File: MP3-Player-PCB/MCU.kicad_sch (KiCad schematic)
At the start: 8 parts, among them J201 Conn_ARM_SWD_TagConnect_TC2030, U201 STM32F411CEUx

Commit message: Up to date
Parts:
- added C207: 100n, symbol Device:C
- added C208: 4.7u, symbol Device:C
- added R201: 10k, symbol Device:R
- C201: value 10u -> 4.7u
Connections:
- net GND: now also U201.23 (VSS), U201.35 (VSS), U201.47 (VSS), U201.49 (VSS), U201.8 (VSSA), C207.2, C208.2, R201.1
- net at U201.22 (VCAP1): now also C208.1
- net BOOT: now reaches U201.44 (BOOT0)
- net BOOT: now also R201.2
- net NRST: now reaches U201.7 (NRST)
- net NRST: now also C207.1

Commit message: Started power schematic
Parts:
- renumbered C201 to C101, C202 to C102, C203 to C103, C204 to C104, C205 to C105, C206 to C106, C207 to C107, C208 to C108, J201 to J101, R201 to R101, U201 to U101
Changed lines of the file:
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@@
 		(dnp no)
 		(fields_autoplaced yes)
-		(property "Reference" "C203"
+		(property "Reference" "C103"
 			(at 63.5 44.4499 0)
 			(effects
@@
 			(project ""
 				(path "/3f51ea9b-d2e1-4711-a47c-269e1b97e0f4/94b81035-f90d-4565-a117-ac4535135684"
-					(reference "C203")
+					(reference "C103")
 					(unit 1)
 				)
@@
 		(dnp no)
 		(fields_autoplaced yes)
-		(property "Reference" "#PWR0206"
+		(property "Reference" "#PWR0105"
 			(at 81.28 147.32 0)
 			(effects
@@
 			(project "MP3-Player"
 				(path "/3f51ea9b-d2e1-4711-a47c-269e1b97e0f4/94b81035-f90d-4565-a117-ac4535135684"
-					(reference "#PWR0206")
+					(reference "#PWR0105")
 					(unit 1)
 				)
@@
 		(on_board yes)
 		(dnp no)
-		(property "Reference" "R201"
+		(property "Reference" "R101"
 			(at 83.82 65.278 90)
 			(effects
@@
 			(project ""
 				(path "/3f51ea9b-d2e1-4711-a47c-269e1b97e0f4/94b81035-f90d-4565-a117-ac4535135684"
-					(reference "R201")
+					(reference "R101")
 					(unit 1)
 				)
@@
 		(dnp no)
 		(fields_autoplaced yes)
-		(property "Reference" "U201"
+		(property "Reference" "U101"
 			(at 115.1733 138.43 0)
 			(effects
@@
 				)
 				(path "/3f51ea9b-d2e1-4711-a47c-269e1b97e0f4/94b81035-f90d-4565-a117-ac4535135684"
-					(reference "U201")
+					(reference "U101")
 					(unit 1)
 				)
@@
 		(dnp no)
 		(fields_autoplaced yes)
-		(property "Reference" "C206"
+		(property "Reference" "C106"
 			(at 97.79 44.4499 0)
 			(effects
@@
 			(project ""
 				(path "/3f51ea9b-d2e1-4711-a47c-269e1b97e0f4/94b81035-f90d-4565-a117-ac4535135684"
-					(reference "C206")
+					(reference "C106")
 					(unit 1)
 				)
@@
 		(dnp no)
 		(fields_autoplaced yes)
-		(property "Reference" "J201"
+		(property "Reference" "J101"
 			(at 207.01 66.0399 0)
 			(effects
@@
 			(project ""
 				(path "/3f51ea9b-d2e1-4711-a47c-269e1b97e0f4/94b81035-f90d-4565-a117-ac4535135684"
-					(reference "J201")
+					(reference "J101")
 					(unit 1)
 				)
@@
 		(dnp no)
 		(fields_autoplaced yes)
-		(property "Reference" "#PWR0204"
+		(property "Reference" "#PWR0103"
 			(at 72.39 80.01 0)
 			(effects
@@
 			(project "MP3-Player"
 				(path "/3f51ea9b-d2e1-4711-a47c-269e1b97e0f4/94b81035-f90d-4565-a117-ac4535135684"
-					(reference "#PWR0204")
+					(reference "#PWR0103")
 					(unit 1)
 				)
@@
 		(dnp no)
 		(fields_autoplaced yes)
-		(property "Reference" "#PWR0201"
+		(property "Reference" "#PWR0102"
 			(at 36.83 59.69 0)
 			(effects
@@
 			(project ""
 				(path "/3f51ea9b-d2e1-4711-a47c-269e1b97e0f4/94b81035-f90d-4565-a117-ac4535135684"
-					(reference "#PWR0201")
+					(reference "#PWR0102")
 					(unit 1)
 				)
@@
 		(dnp no)
 		(fields_autoplaced yes)
-		(property "Reference" "#PWR0203"
+		(property "Reference" "#PWR0106"
 			(at 110.49 147.32 0)
 			(effects
@@
 			(project ""
 				(path "/3f51ea9b-d2e1-4711-a47c-269e1b97e0f4/94b81035-f90d-4565-a117-ac4535135684"
-					(reference "#PWR0203")
+					(reference "#PWR0106")
 					(unit 1)
 				)
@@
 		(dnp no)
 		(fields_autoplaced yes)
-		(property "Reference" "C205"
+		(property "Reference" "C105"
 			(at 86.36 44.4499 0)
 			(effects
@@
 			(project ""
 				(path "/3f51ea9b-d2e1-4711-a47c-269e1b97e0f4/94b81035-f90d-4565-a117-ac4535135684"
-					(reference "C205")
+					(reference "C105")
 					(unit 1)
 				)
@@
 		(dnp no)
 		(fields_autoplaced yes)
-		(property "Reference" "C202"
+		(property "Reference" "C102"
 			(at 52.07 44.4499 0)
 			(effects
@@
 			(project ""
 				(path "/3f51ea9b-d2e1-4711-a47c-269e1b97e0f4/94b81035-f90d-4565-a117-ac4535135684"
-					(reference "C202")
+					(reference "C102")
 					(unit 1)
 				)
@@
 		(dnp no)
 		(fields_autoplaced yes)
-		(property "Reference" "C208"
+		(property "Reference" "C108"
 			(at 85.09 134.6199 0)
 			(effects
@@
 			(project "MP3-Player"
 				(path "/3f51ea9b-d2e1-4711-a47c-269e1b97e0f4/94b81035-f90d-4565-a117-ac4535135684"
-					(reference "C208")
+					(reference "C108")
 					(unit 1)
 				)
@@
 		(dnp no)
 		(fields_autoplaced yes)
-		(property "Reference" "C204"
+		(property "Reference" "C104"
 			(at 74.93 44.4499 0)
 			(effects
@@
 			(project ""
 				(path "/3f51ea9b-d2e1-4711-a47c-269e1b97e0f4/94b81035-f90d-4565-a117-ac4535135684"
-					(reference "C204")
+					(reference "C104")
 					(unit 1)
 				)
@@
 		(dnp no)
 		(fields_autoplaced yes)
-		(property "Reference" "#PWR0202"
+		(property "Reference" "#PWR0101"
 			(at 36.83 40.64 0)
 			(effects
@@
 			(project ""
 				(path "/3f51ea9b-d2e1-4711-a47c-269e1b97e0f4/94b81035-f90d-4565-a117-ac4535135684"
-					(reference "#PWR0202")
+					(reference "#PWR0101")
 					(unit 1)
 				)
@@
 		(dnp no)
 		(fields_autoplaced yes)
-		(property "Reference" "C201"
+		(property "Reference" "C101"
 			(at 40.64 44.4499 0)
 			(effects
@@
 			(project ""
 				(path "/3f51ea9b-d2e1-4711-a47c-269e1b97e0f4/94b81035-f90d-4565-a117-ac4535135684"
-					(reference "C201")
+					(reference "C101")
 					(unit 1)
 				)
@@
 		(on_board yes)
 		(dnp no)
-		(property "Reference" "C207"
+		(property "Reference" "C107"
 			(at 63.754 67.31 0)
 			(effects
@@
 			(project "MP3-Player"
 				(path "/3f51ea9b-d2e1-4711-a47c-269e1b97e0f4/94b81035-f90d-4565-a117-ac4535135684"
-					(reference "C207")
+					(reference "C107")
 					(unit 1)
 				)
@@
 		(dnp no)
 		(fields_autoplaced yes)
-		(property "Reference" "#PWR0205"
+		(property "Reference" "#PWR0104"
 			(at 78.74 80.01 0)
 			(effects
@@
 			(project "MP3-Player"
 				(path "/3f51ea9b-d2e1-4711-a47c-269e1b97e0f4/94b81035-f90d-4565-a117-ac4535135684"
-					(reference "#PWR0205")
-					(unit 1)
-				)
+					(reference "#PWR0104")
+					(unit 1)
+				)

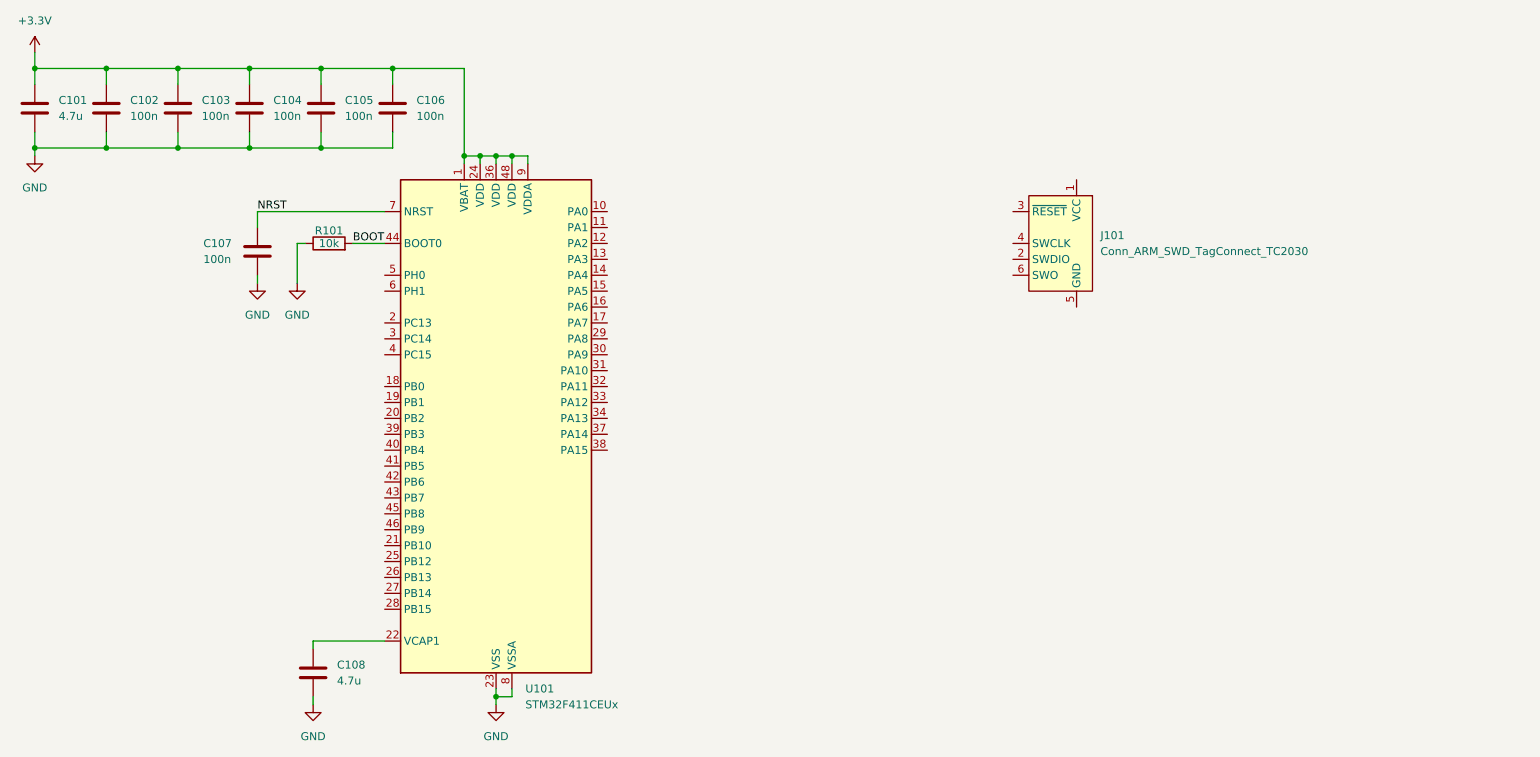
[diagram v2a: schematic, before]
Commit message: Added charger IC schematic circuitry
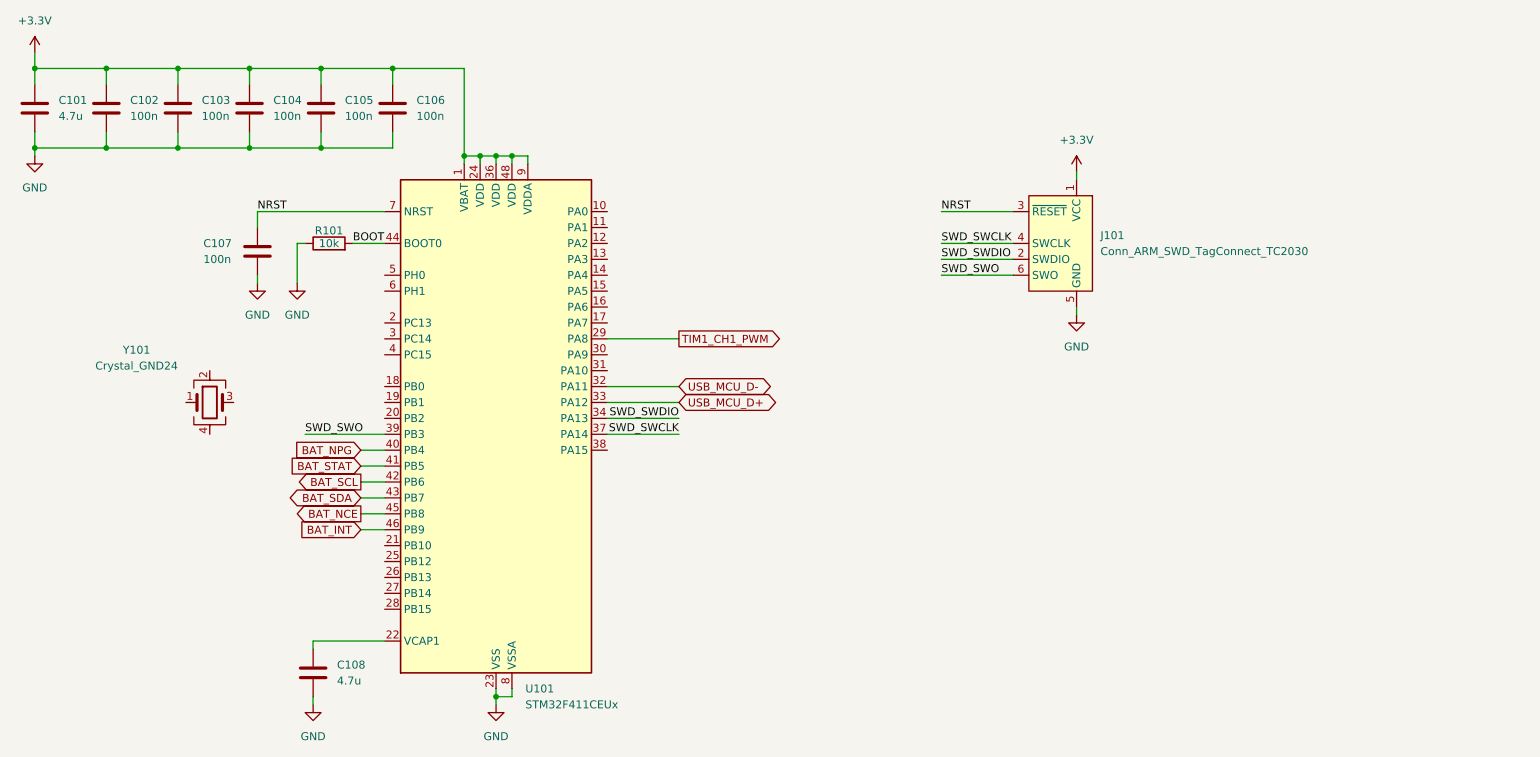
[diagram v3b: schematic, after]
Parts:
- added Y101: Crystal_GND24, symbol Device:Crystal_GND24
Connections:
- net +3.3V: now also J101.1 (VCC)
- net GND: now also J101.5 (GND)
- net NRST: now also J101.3 (~{RESET})
- net TIM1_CH1_PWM: now reaches U101.29 (PA8)
- net USB_MCU_D-: now reaches U101.32 (PA11)
- net USB_MCU_D+: now reaches U101.33 (PA12)
- net SWD_SWDIO: now reaches U101.34 (PA13)
- net SWD_SWDIO: now also J101.2 (SWDIO)
- net SWD_SWCLK: now reaches U101.37 (PA14)
- net SWD_SWCLK: now also J101.4 (SWCLK)
- net SWD_SWO: now reaches U101.39 (PB3)
- net SWD_SWO: now also J101.6 (SWO)
- net BAT_NPG: now reaches U101.40 (PB4)
- net BAT_STAT: now reaches U101.41 (PB5)
- net BAT_SCL: now reaches U101.42 (PB6)
- net BAT_SDA: now reaches U101.43 (PB7)
- net BAT_NCE: now reaches U101.45 (PB8)
- net BAT_INT: now reaches U101.46 (PB9)

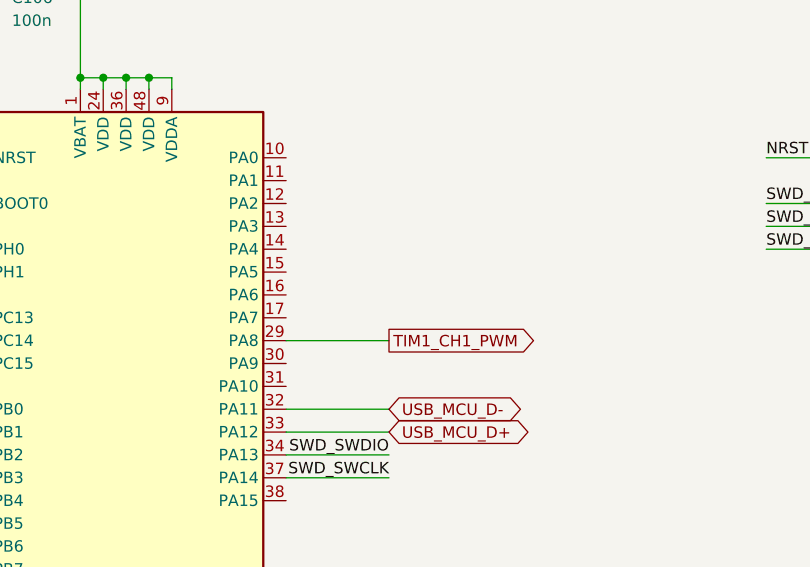
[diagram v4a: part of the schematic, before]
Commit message: Finished SD card connections with MCU
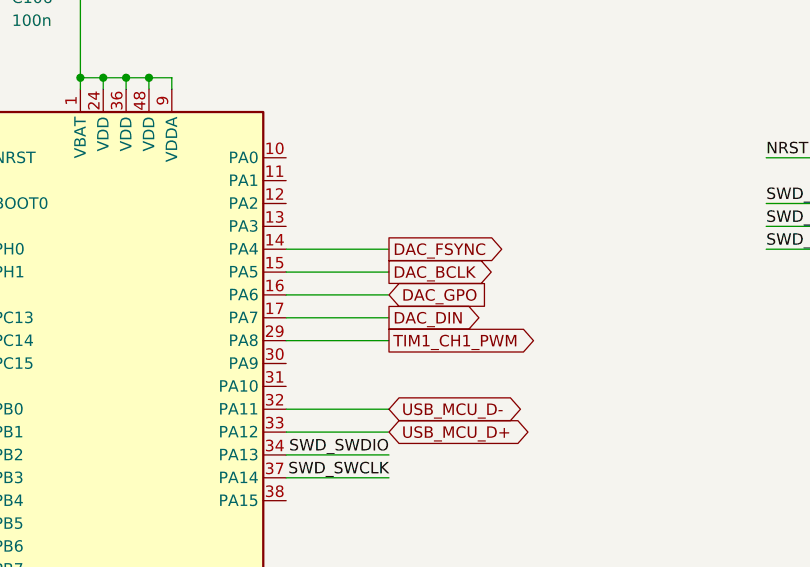
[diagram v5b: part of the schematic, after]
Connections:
- net DAC_FSYNC: now reaches U101.14 (PA4)
- net DAC_BCLK: now reaches U101.15 (PA5)
- net DAC_GPO: now reaches U101.16 (PA6)
- net DAC_DIN: now reaches U101.17 (PA7)
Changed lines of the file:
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@@
+	(wire
+		(pts
+			(xy 128.27 74.93) (xy 139.7 74.93)
+		)
+		(stroke
+			(width 0)
+			(type default)
+		)
+	)
 	(wire
 		(pts
@@
 	(wire
 		(pts
+			(xy 128.27 72.39) (xy 139.7 72.39)
+		)
+		(stroke
+			(width 0)
+			(type default)
+		)
+	)
+	(wire
+		(pts
 			(xy 88.9 102.87) (xy 92.71 102.87)
 		)
@@
 		(pts
 			(xy 81.28 139.7) (xy 81.28 140.97)
+		)
+		(stroke
+			(width 0)
+			(type default)
+		)
+	)
+	(wire
+		(pts
+			(xy 128.27 80.01) (xy 139.7 80.01)
+		)
+		(stroke
+			(width 0)
+			(type default)
+		)
+	)
+	(wire
+		(pts
+			(xy 128.27 77.47) (xy 139.7 77.47)
 		)
 		(stroke
@@
 		)
 	)
+	(global_label "DAC_FSYNC"
+		(shape output)
+		(at 139.7 72.39 0)
+		(fields_autoplaced yes)
+		(effects
+			(font
+				(size 1.27 1.27)
+			)
+			(justify left)
+		)
+		(property "Intersheetrefs" "${INTERSHEET_REFS}"
+			(at 153.2686 72.39 0)
+			(effects
+				(font
+					(size 1.27 1.27)
+				)
+				(justify left)
+				(hide yes)
+			)
+		)
+	)
 	(global_label "BAT_SDA"
 		(shape bidirectional)
@@
 		)
 	)
+	(global_label "DAC_GPO"
+		(shape input)
+		(at 139.7 77.47 0)
+		(fields_autoplaced yes)
+		(effects
+			(font
+				(size 1.27 1.27)
+			)
+			(justify left)
+		)
+		(property "Intersheetrefs" "${INTERSHEET_REFS}"
+			(at 151.1519 77.47 0)
+			(effects
+				(font
+					(size 1.27 1.27)
+				)
+				(justify left)
+				(hide yes)
+			)
+		)
+	)
 	(global_label "TIM1_CH1_PWM"
 		(shape output)
@@
 		)
 	)
+	(global_label "DAC_DIN"
+		(shape output)
+		(at 139.7 80.01 0)
+		(fields_autoplaced yes)
+		(effects
+			(font
+				(size 1.27 1.27)
+			)
+			(justify left)
+		)
+		(property "Intersheetrefs" "${INTERSHEET_REFS}"
+			(at 150.4867 80.01 0)
+			(effects
+				(font
+					(size 1.27 1.27)
+				)
+				(justify left)
+				(hide yes)
+			)
+		)
+	)
 	(global_label "BAT_INT"
 		(shape input)
@@
 				(hide yes)
 			)
+		)
+	)
+	(global_label "DAC_BCLK"
+		(shape output)
+		(at 139.7 74.93 0)
+		(fields_autoplaced yes)
+		(effects
+			(font
+				(size 1.27 1.27)
+			)
+			(justify left)
+		)
+		(property "Intersheetrefs" "${INTERSHEET_REFS}"
+			(at 152.1195 74.93 0)
+			(effects
+				(font
+					(size 1.27 1.27)
+				)
+				(justify left)
+				(hide yes)
+			)

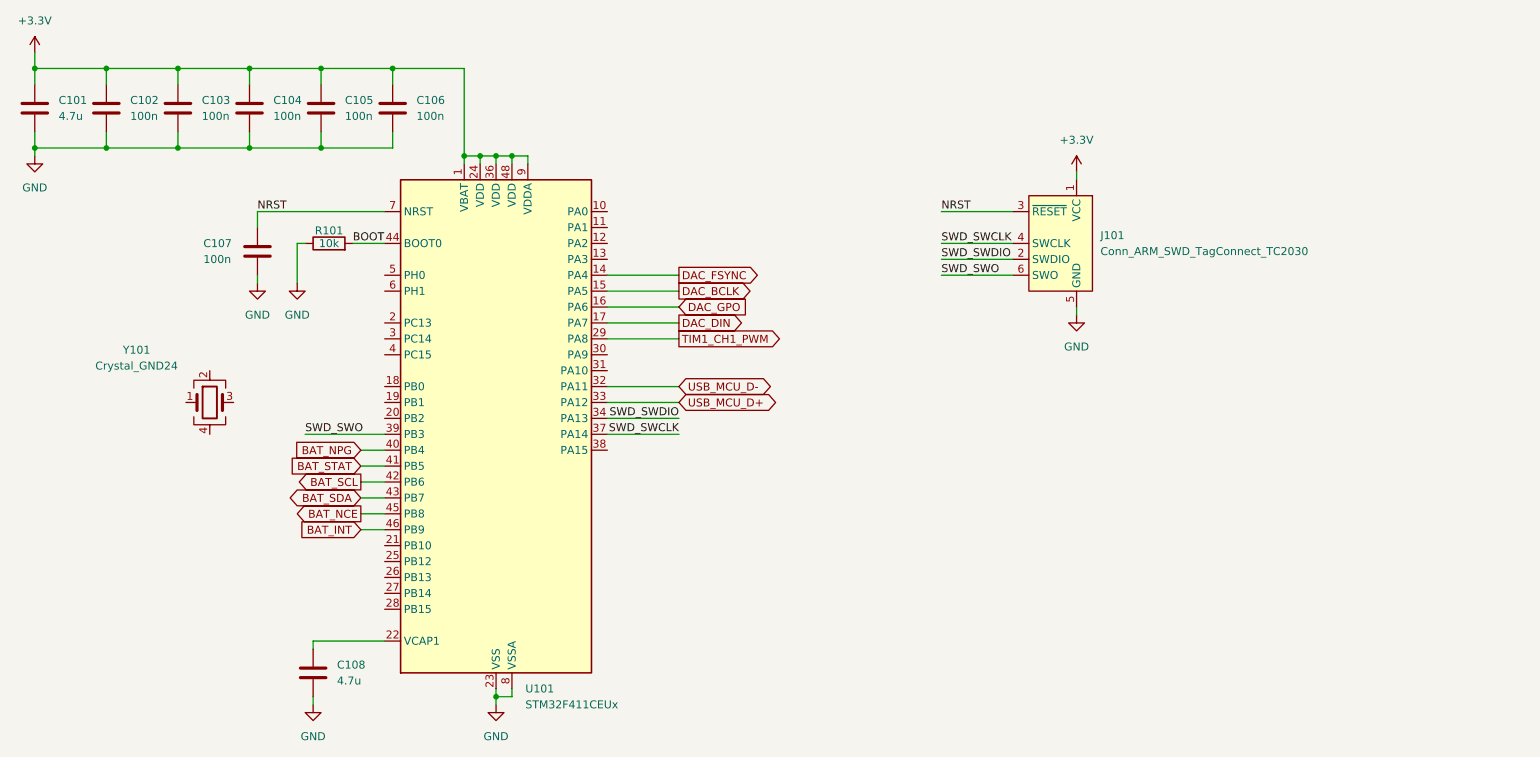
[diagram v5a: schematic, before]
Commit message: Added addressable LED circuitry
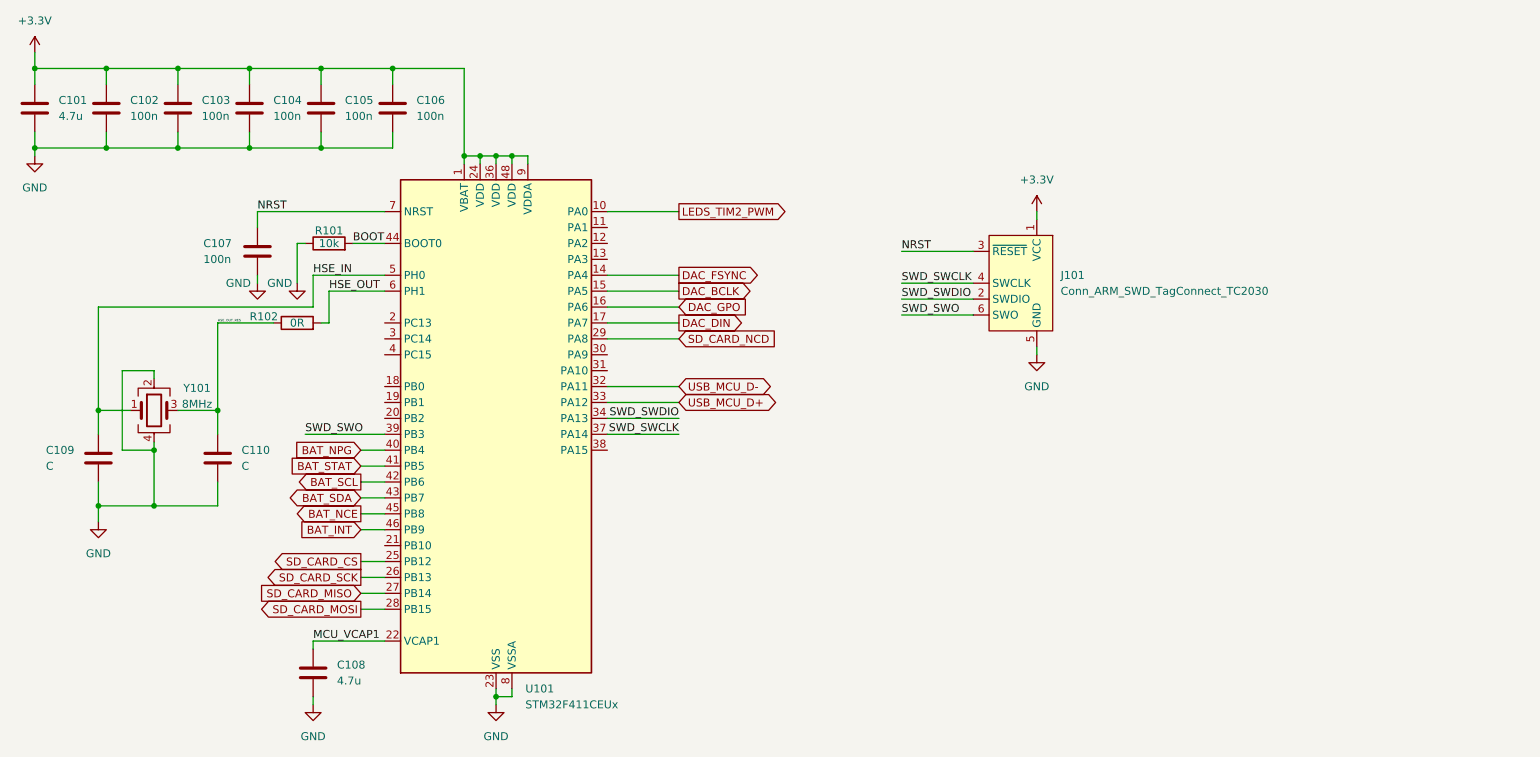
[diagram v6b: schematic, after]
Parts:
- added C109, C110: C, symbol Device:C
- added R102: 0R, symbol Device:R
- Y101: value Crystal_GND24 -> 8MHz
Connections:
- net GND: now also Y101.2, Y101.4, C109.2, C110.2
- net HSE_IN: now reaches Y101.1
- net HSE_IN: now also U101.5 (PH0), C109.1
- net HSE_OUT_RES: now reaches Y101.3
- net HSE_OUT_RES: now also C110.1, R102.1
- net LEDS_TIM2_PWM: now reaches U101.10 (PA0)
- net MCU_VCAP1: now reaches C108.1, U101.22 (VCAP1)
- net SD_CARD_CS: now reaches U101.25 (PB12)
- net SD_CARD_SCK: now reaches U101.26 (PB13)
- net SD_CARD_MISO: now reaches U101.27 (PB14)
- net SD_CARD_MOSI: now reaches U101.28 (PB15)
- net HSE_OUT: now reaches U101.6 (PH1)
- net HSE_OUT: now also R102.2
- net TIM1_CH1_PWM renamed SD_CARD_NCD
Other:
- moved on the sheet: J101, Y101
